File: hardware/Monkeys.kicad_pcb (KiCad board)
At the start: 2 copper layers, 144.9 x 59.8 mm, 137 parts, among them IC1 SI4702-C19-GM, J1 EXT 5V, J2 3.3vSerial, J3 Therm, J4 PJ-320D-4A, J5 10118194-0001LF, Q1 BSS138, Q2 SI2302, Q3 MMBT3904, Q4 MMBT3904, Q5 MMBT3904, Q6 MMBT3904, SW1 SW_Push, SW2 SW_Push, SW3 SW_Push, SW4 SW_Push, U1 BQ24072RGT, U2 RT9080-33GJ5, U3 CH340C, U4 LMV358, U5 InfraredReceiver, U6 ESP32-WROOM-32E(8MB)

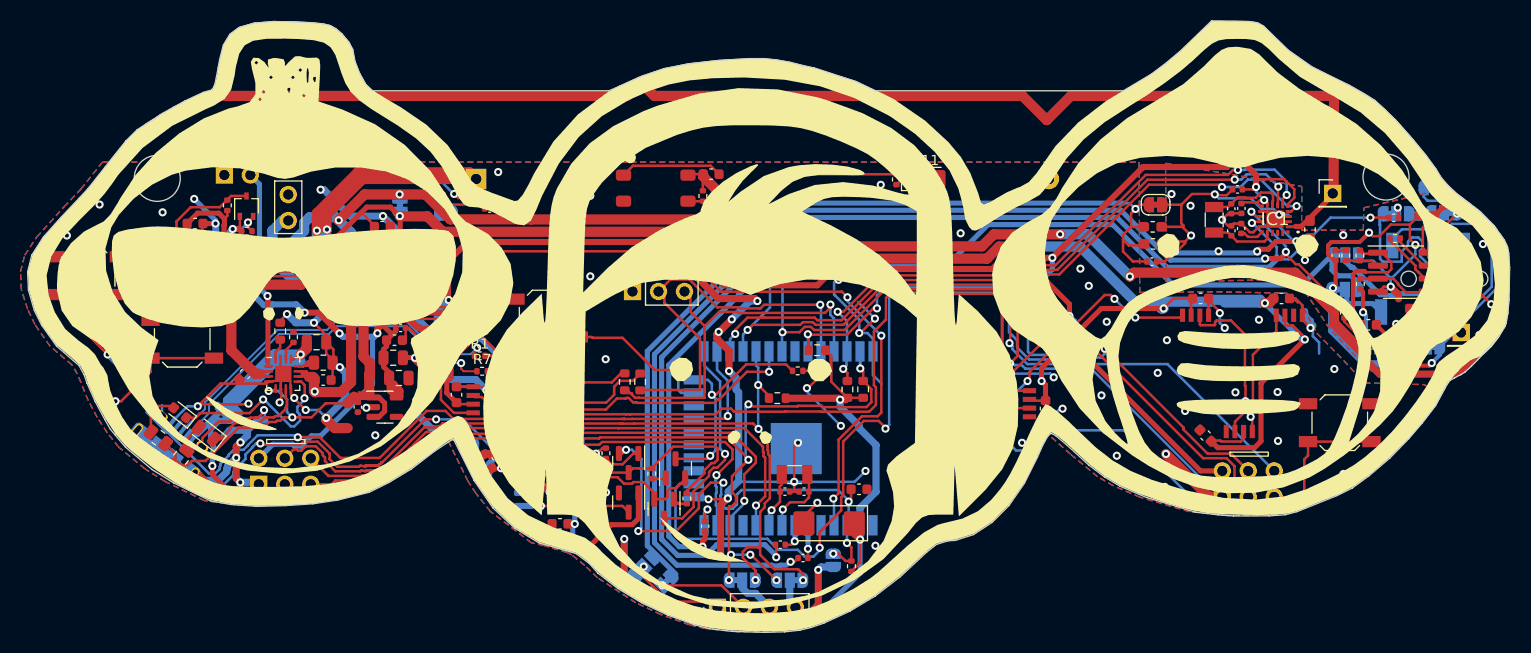
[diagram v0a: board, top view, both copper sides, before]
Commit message: hardware: Badge revision v2.2
After some initial testing we came up with a number of errata as noted
here.  These changes have been implemented:

- Need to replace the infrared LED emitter with one that is
  front-facing, and doesn’t require hand-soldering.
- Make a true reset button
- Replace the audio connector with a thru-hole for strength
- Tent the vias so white is white
- Drag a few more parts off of the silk
- Figure out a better way to do powered-off re-charge

This spin of the hardware went to initial manufacturing with the gerbers
provided on November 30th, 2022.
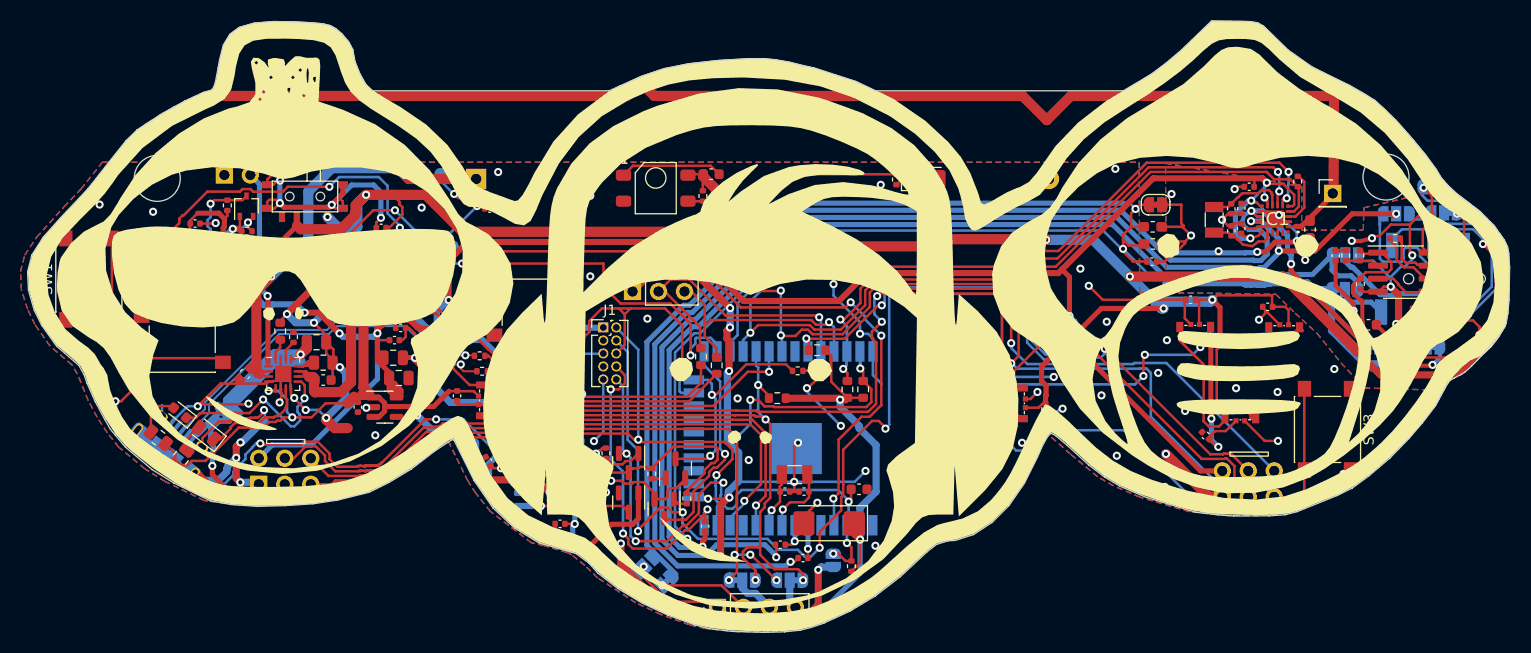
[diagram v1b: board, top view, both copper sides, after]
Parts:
- removed C10, C11: 1uF, Capacitor_SMD:C_0402_1005Metric
- removed C16: 4.7uF, Capacitor_SMD:C_0603_1608Metric
- removed JP2: Use VDC for Lights, Jumper:SolderJumper-2_P1.3mm_Bridged_RoundedPad1.0x1.5mm
- removed JP8: Power On/Off, Connector_PinHeader_2.54mm:PinHeader_1x03_P2.54mm_Vertical
- removed TP6: TP, Connector_PinHeader_2.54mm:PinHeader_1x01_P2.54mm_Vertical
- added R36: 10K, monkeys20221112:R_0402_1005Metric, F.Cu at (202.1, 64.8)
- added SW5: SPDT_Switch_Grounded, monkeys20221112:SPDT Switch MSK12C02-HB, F.Cu at (105.0, 66.3)
- BT1: footprint JTFooties:1xAA -> monkeys20221112:1xAA
- C1, C21, C22, C23, C24, C26, C28, C3, C32, C36, C37, C39, C41, C5, C8, C9: footprint Capacitor_SMD:C_0402_1005Metric -> monkeys20221112:C_0402_1005Metric
- C12, C17, C18, C19, C20, C25, C31, C38, C4, C6, C7: footprint Capacitor_SMD:C_0603_1608Metric -> monkeys20221112:C_0402_1005Metric
- C13, C15, C27, C34, C35, C40: footprint Capacitor_SMD:C_0603_1608Metric -> monkeys20221112:C_0603_1608Metric
- C14: value 10uF -> 1uF; footprint Capacitor_SMD:C_0603_1608Metric -> monkeys20221112:C_0402_1005Metric
- C2: footprint Capacitor_Tantalum_SMD:CP_EIA-6032-20_AVX-F -> monkeys20221112:CP_EIA-6032-20_AVX-F
- C29, C30, C33: footprint Capacitor_SMD:C_0805_2012Metric -> monkeys20221112:C_0805_2012Metric
- D1: footprint LED_SMD:LED_0402_1005Metric -> monkeys20221112:LED_0402_1005Metric
- D10: footprint LED_SMD:LED_0603_1608Metric -> monkeys20221112:LED_0603_1608Metric
- D11: footprint LED_SMD:LED_1206_3216Metric -> monkeys20221112:LED_1206_3216Metric
- D2, D3, D4, D5, D6, D7, D8: value WS2812B-4020 -> SK6812D-EC3210R; footprint JTFooties:WS2812B-4020 -> monkeys20221112:SK6812D-EC3210R
- D9: footprint LED_SMD:LED_0805_2012Metric -> monkeys20221112:LED_0805_2012Metric
- G***: footprint JTFooties:monkeysilk -> monkeys20221112:monkeysilk
- H1, H2: footprint MountingHole:MountingHole_4.5mm -> monkeys20221112:MountingHole_4.5mm
- IC1: footprint SamacSys_Parts:SI4702C19GM -> monkeys20221112:SI4702C19GM
- J1: value EXT 5V -> JTAG; footprint Connector_PinHeader_2.54mm:PinHeader_1x02_P2.54mm_Vertical -> monkeys20221112:PinHeader_2x05_P1.27mm_Vertical
- J2: footprint Connector_PinSocket_2.54mm:PinSocket_1x03_P2.54mm_Vertical -> monkeys20221112:PinSocket_1x03_P2.54mm_Vertical
- J3: footprint Connector_PinHeader_2.54mm:PinHeader_1x02_P2.54mm_Vertical -> monkeys20221112:PinHeader_1x02_P2.54mm_Vertical
- J4: footprint Connector_Audio:Jack_3.5mm_PJ320D_Horizontal -> monkeys20221112:Jack_3.5mm_PJ320D_Horizontal
- J5: footprint JTFooties:AMPHENOL_10118194-0001LF_JT -> monkeys20221112:AMPHENOL_10118194-0001LF_JT
- JP1: footprint Jumper:SolderJumper-2_P1.3mm_Open_RoundedPad1.0x1.5mm -> monkeys20221112:SolderJumper-2_P1.3mm_Open_RoundedPad1.0x1.5mm
- JP10, JP12, JP13, JP14, JP15, JP3, JP4, JP5, JP6, JP9: footprint Jumper:SolderJumper-3_P1.3mm_Bridged12_RoundedPad1.0x1.5mm -> monkeys20221112:SolderJumper-3_P1.3mm_Bridged12_RoundedPad1.0x1.5mm
- JP7, R25, R32, R35: footprint Jumper:SolderJumper-2_P1.3mm_Bridged_RoundedPad1.0x1.5mm -> monkeys20221112:SolderJumper-2_P1.3mm_Bridged_RoundedPad1.0x1.5mm
- L1, L2, L3: footprint Inductor_SMD:L_0603_1608Metric_Pad1.05x0.95mm_HandSolder -> monkeys20221112:L_0603_1608Metric_Pad1.05x0.95mm_HandSolder
- LCD1: footprint Connector_PinHeader_2.54mm:PinHeader_1x04_P2.54mm_Vertical -> monkeys20221112:PinHeader_1x04_P2.54mm_Vertical
- Q1: footprint Package_TO_SOT_SMD:SOT-323_SC-70 -> monkeys20221112:SOT-323_SC-70
- Q2, Q3, Q4, Q5, Q6: footprint Package_TO_SOT_SMD:SOT-23 -> monkeys20221112:SOT-23
- R1, R12, R13, R19, R20, R21, R22, R23, R24, R31, R33, R34, R5, R7: footprint Resistor_SMD:R_0402_1005Metric -> monkeys20221112:R_0402_1005Metric
- R10, R30: value 470 -> 470R; footprint Resistor_SMD:R_0402_1005Metric -> monkeys20221112:R_0402_1005Metric
- R11, R15: value 10K -> 20K; footprint Resistor_SMD:R_0402_1005Metric -> monkeys20221112:R_0402_1005Metric
- R14, R16: value 10K -> 3.9K; footprint Resistor_SMD:R_0402_1005Metric -> monkeys20221112:R_0402_1005Metric
- R17, R18: value 33K -> 3.9K; footprint Resistor_SMD:R_0402_1005Metric -> monkeys20221112:R_0402_1005Metric
- R2, R4, R6: footprint Resistor_SMD:R_0805_2012Metric -> monkeys20221112:R_0805_2012Metric
- R26, R27, R28, R29, R3, R8, R9: footprint Resistor_SMD:R_0603_1608Metric -> monkeys20221112:R_0603_1608Metric
- SAO1, SAO2: footprint JTFooties:ShittyAddOn_Female -> monkeys20221112:ShittyAddOn_Female
- SW1, SW2, SW3, SW4: footprint Button_Switch_SMD:SW_SPST_SKQG_WithStem -> monkeys20221112:SW_SPST_PTS645
- TP1: footprint Connector_PinHeader_2.54mm:PinHeader_1x01_P2.54mm_Vertical -> monkeys20221112:PinHeader_1x01_P2.54mm_Vertical
- U1: footprint Package_DFN_QFN:VQFN-16-1EP_3x3mm_P0.5mm_EP1.6x1.6mm -> monkeys20221112:VQFN-16-1EP_3x3mm_P0.5mm_EP1.6x1.6mm
- U2: footprint Package_TO_SOT_SMD:SOT-23-5 -> monkeys20221112:SOT-23-5
- U3: footprint Package_SO:SOIC-16_3.9x9.9mm_P1.27mm -> monkeys20221112:SOIC-16_3.9x9.9mm_P1.27mm
- U4: value LMV358 -> LM4808; footprint Package_SO:SOIC-8_3.9x4.9mm_P1.27mm -> monkeys20221112:SOIC-8_3.9x4.9mm_P1.27mm
- U5: footprint JTFooties:IRM-H638T-TR2 -> monkeys20221112:IRM-H638T-TR2
- U6: footprint RF_Module:ESP32-WROOM-32 -> monkeys20221112:ESP32-WROOM-32
- Y1, Y2: footprint Crystal:Crystal_SMD_3215-2Pin_3.2x1.5mm -> monkeys20221112:Crystal_SMD_3215-2Pin_3.2x1.5mm
- moved J1 17.8 mm to (134.2, 79.1), turned to 0 degrees
- moved C8 9.67 mm to (218.6, 74.9), turned to -90 degrees
- moved R9 9.13 mm to (145.3, 82.8), turned to 90 degrees
- moved R8 6.45 mm to (143.8, 81.9), turned to 90 degrees
- moved C9 5.67 mm to (205.8, 72.0), turned to -90 degrees
- moved R11 4.47 mm to (217.1, 71.9), turned to 180 degrees
- moved R35 3.44 mm to (118.9, 71.3)
- moved C20 1.59 mm to (199.2, 77.0), turned to 0 degrees
- moved SW3 1.37 mm to (205.0, 89.0), turned to -90 degrees
- moved SW4 1.31 mm to (127.5, 77.6)
- moved C21 1.17 mm to (197.4, 65.3)
- moved C18 0.99 mm to (191.6, 76.3), turned to 0 degrees
- moved D8 0.94 mm to (200.8, 79.4)
- moved D7 0.93 mm to (196.5, 87.5)
- moved D6 0.79 mm to (192.1, 79.4)
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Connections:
- C12 pad 2: /RGB_PWR -> +VDC
- C17 pad 2: /RGB_PWR -> +VDC
- C18 pad 2: /RGB_PWR -> +VDC
- C19 pad 2: /RGB_PWR -> +VDC
- C20 pad 2: /RGB_PWR -> +VDC
- C32 pad 2: Net-(C32-Pad2) -> /IO12
- C39 pad 2: /DFS -> +3V3
- C4 pad 2: /RGB_PWR -> +VDC
- C6 pad 2: /RGB_PWR -> +VDC
- C7 pad 2: +VDC -> Net-(C7-Pad2)
- C8 pad 2: /LOUT -> Net-(C8-Pad2)
- C9 pad 2: /ROUT -> Net-(C9-Pad2)
- D2 pad 1: Net-(D2-Pad1) -> GND
- D2 pad 2: /RGB_PWR -> Net-(D2-Pad2)
- D2 pad 4: GND -> +VDC
- D3 pad 1: Net-(D2-Pad3) -> GND
- D3 pad 2: /RGB_PWR -> Net-(D3-Pad2)
- D3 pad 3: Net-(D3-Pad3) -> Net-(D2-Pad2)
- D3 pad 4: GND -> +VDC
- D4 pad 1: Net-(D3-Pad3) -> GND
- D4 pad 2: /RGB_PWR -> Net-(D4-Pad2)
- D4 pad 3: Net-(D4-Pad3) -> Net-(D3-Pad2)
- D4 pad 4: GND -> +VDC
- D5 pad 1: Net-(D4-Pad3) -> GND
- D5 pad 2: /RGB_PWR -> Net-(D5-Pad2)
- D5 pad 3: Net-(D5-Pad3) -> Net-(D4-Pad2)
- D5 pad 4: GND -> +VDC
- D6 pad 1: Net-(D5-Pad3) -> GND
- D6 pad 2: /RGB_PWR -> Net-(D6-Pad2)
- D6 pad 3: Net-(D6-Pad3) -> Net-(D5-Pad2)
- D6 pad 4: GND -> +VDC
- D7 pad 1: Net-(D6-Pad3) -> GND
- D7 pad 2: /RGB_PWR -> Net-(D7-Pad2)
- D7 pad 3: Net-(D7-Pad3) -> Net-(D6-Pad2)
- D7 pad 4: GND -> +VDC
- D8 pad 1: Net-(D7-Pad3) -> GND
- D8 pad 2: /RGB_PWR -> unconnected-(D8-Pad2)
- D8 pad 3: unconnected-(D8-Pad3) -> Net-(D7-Pad2)
- D8 pad 4: GND -> +VDC
- IC1 pad 16: /DFS -> +3V3
- J1 pad 1: /RGB_PWR -> +3V3
- J1 pad 2: GND -> /T6_DOWN
- JP3 pad 1: Net-(JP3-Pad1) -> Net-(C8-Pad2)
- JP3 pad 2: Net-(C8-Pad1) -> /LOUT
- JP4 pad 1: Net-(JP4-Pad1) -> Net-(C9-Pad2)
- JP4 pad 2: Net-(C9-Pad1) -> /ROUT
- JP7 pad 1: Net-(JP7-Pad1) -> Net-(C7-Pad2)
- Q1 pad 3: Net-(D2-Pad1) -> Net-(D2-Pad3)
- R11 pad 1: Net-(JP3-Pad1) -> GNDA
- R11 pad 2: /VREF -> Net-(C13-Pad1)
- R13 pad 1: Net-(D2-Pad1) -> Net-(D2-Pad3)
- R13 pad 2: /RGB_PWR -> +VDC
- R14 pad 1: Net-(C10-Pad1) -> Net-(C8-Pad1)
- R15 pad 1: Net-(JP4-Pad1) -> GNDA
- R15 pad 2: /VREF -> Net-(C15-Pad1)
- R16 pad 1: Net-(C11-Pad1) -> Net-(C9-Pad1)
- R23 pad 1: Net-(JP7-Pad1) -> Net-(C7-Pad2)
- U4 pad 8: +VDC -> Net-(C7-Pad2)
- U6 pad 14: Net-(C32-Pad2) -> /IO12
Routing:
- net /RGB_PWR: track 210.7 -> 0.00 mm, vias 6 -> 0
- net GND: track 453.3 -> 548.3 mm, vias 97 -> 101
- net +VDC: track 225.2 -> 316.6 mm, vias 8 -> 11
- net Net-(D4-Pad2): track 0.00 -> 76.1 mm, vias 0 -> 2
- net Net-(D4-Pad3): track 74.9 -> 0.00 mm
- net GNDA: track 103.1 -> 140.5 mm, vias 25 -> 22
- net Net-(C7-Pad2): track 0.00 -> 32.5 mm, vias 0 -> 2
- net /IO12: track 0.00 -> 32.0 mm, vias 0 -> 3
- net Net-(D2-Pad2): track 0.00 -> 31.9 mm, vias 0 -> 2
- net /BATT: track 71.4 -> 42.9 mm, vias 4 -> 2
- net Net-(D3-Pad3): track 26.1 -> 0.00 mm
- net Net-(D5-Pad2): track 0.00 -> 25.2 mm, vias 0 -> 4
- net Net-(JP7-Pad1): track 24.8 -> 0.00 mm, vias 1 -> 0
- net Net-(D5-Pad3): track 24.8 -> 0.00 mm, vias 4 -> 0
- net Net-(D3-Pad2): track 0.00 -> 22.2 mm
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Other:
- board text added: "Monkeybadge 2.2 For Hushcon Designed Jan-Nov 2022 By PacketChat, a California Small Corporation"
- board text added: "Temtel Crackerjack Redbeard"
- board text removed: "DNP"
- board text removed: "Monkeybadge 2.0 For Hushcon Seattle Designed Jan-Aug 2022 By PacketChat, a California Small Business"
- board text removed: "Temtel, Crackerjack Redbeard"

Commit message: hardware: Badge revision 3.4
After a holiday break work on revision 3.4 of the Monkey badge began
March 24th, 2023.

In this revision changes were made to the following components:
- power regulator
- Charge/powerpath controller
- the headphone jack
- Resistor/capacitor values on the LM4808 amplifer
- Removal of experimental touch pads

This spin of the hardware went to initial manufacturing with the gerbers
provided on July 25th, 2023.
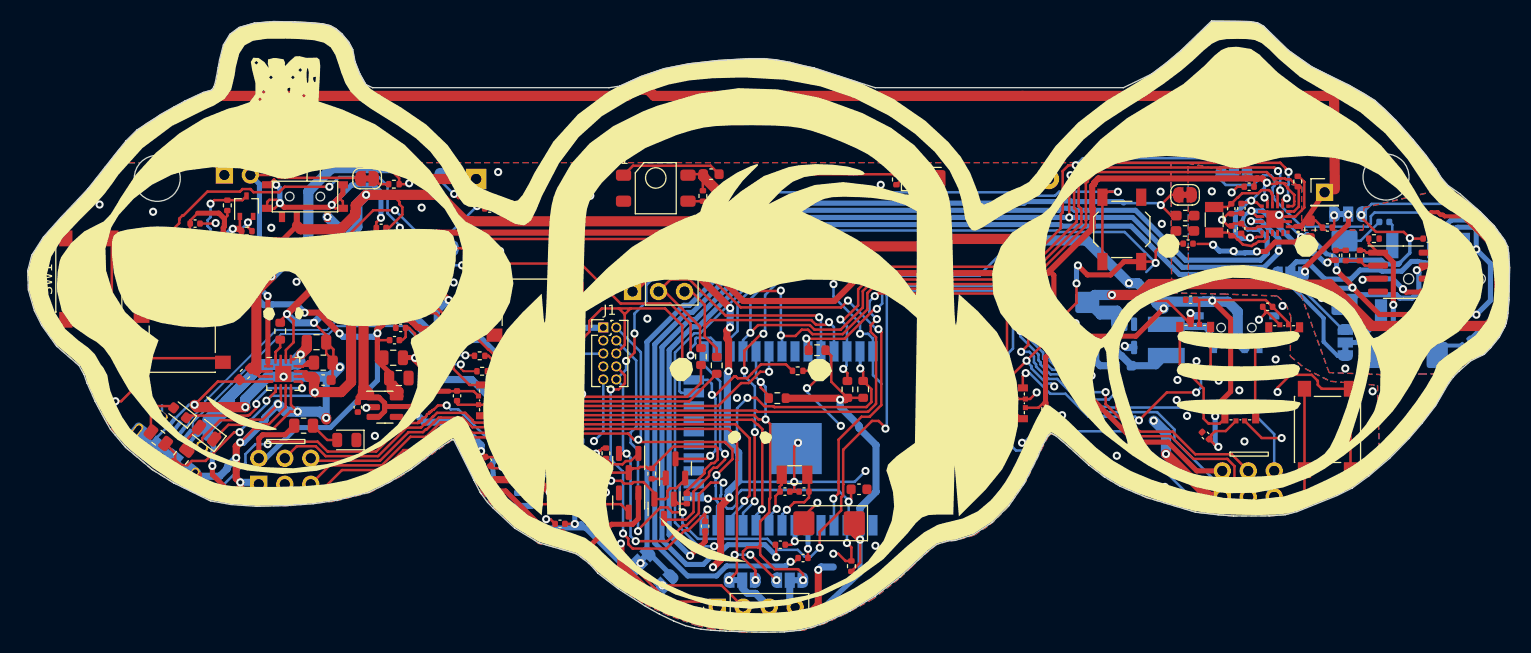
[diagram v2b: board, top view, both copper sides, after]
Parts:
- removed JP4: RBypassA, monkeys20221112:SolderJumper-3_P1.3mm_Bridged12_RoundedPad1.0x1.5mm
- removed JP5: LBypass2, monkeys20221112:SolderJumper-3_P1.3mm_Bridged12_RoundedPad1.0x1.5mm
- removed JP6: RBypassB, monkeys20221112:SolderJumper-3_P1.3mm_Bridged12_RoundedPad1.0x1.5mm
- removed JP7: Amp Power Disable, monkeys20221112:SolderJumper-2_P1.3mm_Bridged_RoundedPad1.0x1.5mm
- added C10: 10uF, monkeys20221112:C_0603_1608Metric, B.Cu at (185.1, 82.8)
- added C11: 100uF, monkeys20221112:CP_EIA-6032-20_AVX-F, B.Cu at (181.5, 79.1)
- added C16: 330uF, Capacitor_Tantalum_SMD:CP_EIA-7343-31_Kemet-D, B.Cu at (212.6, 81.8)
- added D12: Green, monkeys20221112:LED_0805_2012Metric, F.Cu at (109.1, 90.1)
- added FB1: SCBG100505U801T, Inductor_SMD:L_0402_1005Metric, B.Cu at (218.6, 80.5)
- added FB2: SCBG100505U801T, Inductor_SMD:L_0402_1005Metric, B.Cu at (210.6, 68.7)
- added G***: LOGO, JTFooties:hushconlogo, B.Cu at (93.6, 76.6)
- added JP2: ANT/GNDA, monkeys20221112:SolderJumper-3_P1.3mm_Bridged12_RoundedPad1.0x1.5mm, B.Cu at (207.0, 68.0)
- added L4: 22uH, Inductor_SMD:L_Bourns-SRN4018, B.Cu at (189.3, 80.3)
- added R37: 10K, monkeys20221112:R_0402_1005Metric, F.Cu at (113.7, 65.0)
- added SW6: SW_MEC_5E, JTFooties:Button_metal, F.Cu at (184.9, 69.5)
- added SW7: SPDT_Switch, monkeys20221112:SPDT Switch MSK12C02-HB, B.Cu at (195.8, 77.9)
- added U7: Boost5V, Package_TO_SOT_SMD:SOT-23-5, B.Cu at (185.2, 79.9)
- BT1: footprint monkeys20221112:1xAA -> JTFooties:1xAA_NUB
- C13: value 10uF -> 330uF; footprint monkeys20221112:C_0603_1608Metric -> Capacitor_Tantalum_SMD:CP_EIA-7343-31_Kemet-D; moved to B.Cu
- C15: value 10uF -> 100pF; footprint monkeys20221112:C_0603_1608Metric -> Capacitor_SMD:C_0402_1005Metric
- C8, C9: value 1uF -> 390nF
- JP1: value RESET -> EXT Therm; footprint monkeys20221112:SolderJumper-2_P1.3mm_Open_RoundedPad1.0x1.5mm -> Jumper:SolderJumper-2_P1.3mm_Bridged_RoundedPad1.0x1.5mm; moved to F.Cu
- JP10: value MIC/GND -> MIC/GNDA
- JP3: value LBypass1 -> PWMLOUT
- JP9: value GND/MIC -> GNDA/MIC
- LCD1: footprint monkeys20221112:PinHeader_1x04_P2.54mm_Vertical -> Connector_PinHeader_2.54mm:PinHeader_1x04_P2.54mm_Vertical
- R14, R16: value 3.9K -> 20K
- R17, R18: value 3.9K -> 30K
- R5: value 46.4K -> 1K; footprint monkeys20221112:R_0402_1005Metric -> monkeys20221112:R_0805_2012Metric
- SW5: value SPDT_Switch_Grounded -> SPDT_Switch
- moved JP1 58.9 mm to (111.1, 64.5), turned to 0 degrees
- moved JP3 16.3 mm to (195.9, 64.0)
- moved C13 11.0 mm to (206.7, 73.7), turned to 90 degrees
- moved C15 10.3 mm to (205.0, 69.3)
- moved R5 8.71 mm to (104.9, 88.7), turned to 180 degrees
- moved R17 6.34 mm to (217.2, 73.4)
- moved JP9 5.69 mm to (201.4, 73.8), turned to 180 degrees
- moved JP10 5.18 mm to (206.8, 80.5), turned to 90 degrees
- moved R15 4.63 mm to (209.6, 70.4), turned to 180 degrees
- moved R23 4.20 mm to (217.2, 76.5)
- moved C26 3.95 mm to (191.4, 70.9)
- moved R24 3.89 mm to (215.2, 76.9)
- moved C14 3.73 mm to (217.2, 75.5), turned to 180 degrees
- moved L3 3.37 mm to (191.1, 69.6)
- moved L2 3.37 mm to (191.1, 68.1)
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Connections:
- net Net-(C7-Pad2) renamed +5V
- C15 pad 1: Net-(C15-Pad1) -> /FMIP
- C15 pad 2: /RAUD -> Net-(C15-Pad2)
- C35 pad 1: Net-(C35-Pad1) -> /OUT
- C9 pad 2: Net-(C9-Pad2) -> /ROUT
- IC1 pad 2: Net-(AE1-Pad1) -> /FMIP
- JP1 pad 1: /RST -> /THERM
- JP1 pad 2: GND -> Net-(JP1-Pad2)
- JP10 pad 1: GNDA -> /MIC
- JP10 pad 3: /MIC -> Net-(JP10-Pad3)
- JP12 pad 1: +3V3 -> GND
- JP12 pad 3: GND -> +3V3
- JP13 pad 1: GND -> +3V3
- JP13 pad 3: +3V3 -> GND
- JP3 pad 3: /LBP -> /PWMLOUT
- JP9 pad 1: /MIC -> Net-(JP10-Pad3)
- JP9 pad 3: GNDA -> /MIC
- L1 pad 2: Net-(AE1-Pad1) -> /FMIP
- R15 pad 2: Net-(C15-Pad1) -> Net-(C16-Pad1)
- R18 pad 1: Net-(C15-Pad1) -> Net-(C16-Pad1)
- R4 pad 2: +VDC -> /OUT
- R5 pad 1: GND -> Net-(D12-Pad2)
- R5 pad 2: Net-(R5-Pad2) -> +3V3
- R6 pad 2: +VDC -> /OUT
- SW5 pad 1: Net-(C35-Pad1) -> /OUT
- TP1 pad 1: Net-(AE1-Pad1) -> /FMIP
- U1 pad 10: Net-(C35-Pad1) -> /OUT
- U1 pad 11: Net-(C35-Pad1) -> /OUT
- U1 pad 14: Net-(R5-Pad2) -> GND
- U1 pad 5: +VDC -> /OUT
- U4 pad 1: Net-(C15-Pad1) -> Net-(C16-Pad1)
- U6 pad 11: /IO26_INFRARCV -> /PWMLOUT
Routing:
- net Net-(AE1-Pad1): track 127.5 -> 0.00 mm
- net /FMIP: track 0.00 -> 125.5 mm
- net /PWMLOUT: track 0.00 -> 81.8 mm, vias 0 -> 6
- net +VDC: track 316.6 -> 235.0 mm, vias 11 -> 8
- net /RST: track 55.0 -> 124.8 mm, vias 6 -> 9
- net GND: track 548.3 -> 611.9 mm, vias 101 -> 117
- net /OUT: track 0.00 -> 47.3 mm, vias 0 -> 5
- net GNDA: track 140.5 -> 96.2 mm, vias 22 -> 21
- net +5V: track 32.5 -> 72.5 mm, vias 2 -> 1
- net Net-(C35-Pad1): track 26.5 -> 0.00 mm, vias 2 -> 0
- net Net-(C8-Pad2): track 16.5 -> 33.4 mm
- net Net-(C16-Pad1): track 0.00 -> 15.3 mm, vias 0 -> 1
- net Net-(JP10-Pad3): track 0.00 -> 14.6 mm, vias 0 -> 2
- net Net-(C15-Pad1): track 12.2 -> 0.00 mm
- net +3V3: track 327.1 -> 339.3 mm
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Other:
- outline, holes or cut-outs redrawn
- board text added: "+"
- board text added: "-"
- board text added: "Headphone Amp 5V"
- board text added: "Monkeybadge 3.4 Designed Jan 2022 - July 2023 By PacketChat, a California Small Corporation"
- board text added: "Negative Side!!!"
- board text added: "Positive Side!!!"
- board text added: "Temtel Redbeard Crackerjack Paul"
- board text removed: "Copyright 2022 PacketChat"
- board text removed: "Monkeybadge 2.2 For Hushcon Designed Jan-Nov 2022 By PacketChat, a California Small Corporation"
- board text removed: "Temtel Crackerjack Redbeard"
